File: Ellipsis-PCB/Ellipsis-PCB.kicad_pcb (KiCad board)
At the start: 2 copper layers, 114.3 x 102.4 mm, 71 parts, among them J1 Ex_Bat, J2 USB, J3 SWD, J4 Conn_02x05_Counter_Clockwise, J5 Conn_02x05_Counter_Clockwise, Q1 AO3407, Q2 AO3407, U1 E73-2G4M08S1C-52840, U2 XC6220B331MR-G, U3 MCP73831-3-OT

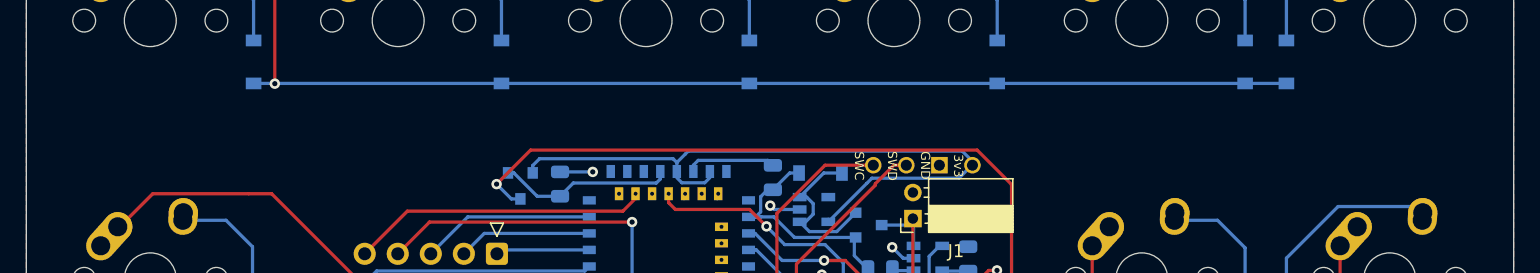
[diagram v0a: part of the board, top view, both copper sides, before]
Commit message: More things
Added mousebites and the right half
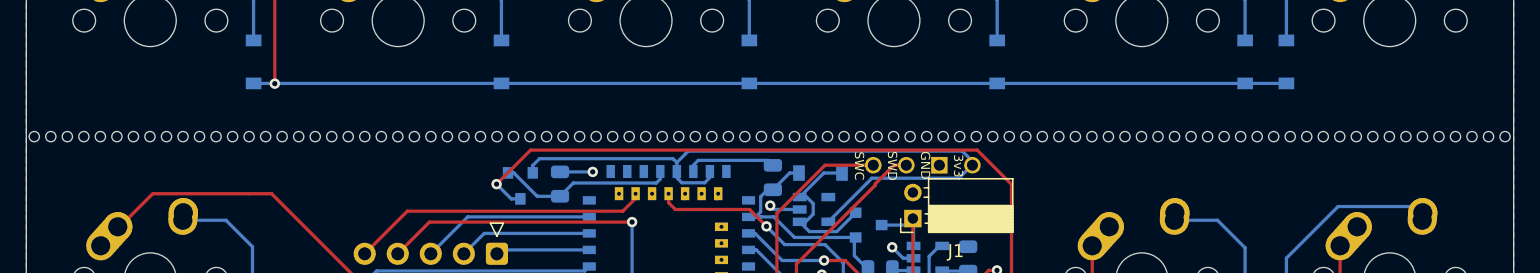
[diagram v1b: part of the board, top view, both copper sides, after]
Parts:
- added REF**: breakaway-mousebites, random-keyboard-parts:breakaway-mousebites, F.Cu at (96.0, 267.1)
- added REF**: breakaway-mousebites, random-keyboard-parts:breakaway-mousebites, F.Cu at (38.9, 267.1)
- added REF**: breakaway-mousebites, random-keyboard-parts:breakaway-mousebites, F.Cu at (51.6, 267.1)
- added REF**: breakaway-mousebites, random-keyboard-parts:breakaway-mousebites, F.Cu at (45.2, 267.1)
- added REF**: breakaway-mousebites, random-keyboard-parts:breakaway-mousebites, F.Cu at (19.8, 267.1)
- added REF**: breakaway-mousebites, random-keyboard-parts:breakaway-mousebites, F.Cu at (32.5, 267.1)
- added REF**: breakaway-mousebites, random-keyboard-parts:breakaway-mousebites, F.Cu at (26.2, 267.1)
- added REF**: breakaway-mousebites, random-keyboard-parts:breakaway-mousebites, F.Cu at (0.77, 267.1)
- added REF**: breakaway-mousebites, random-keyboard-parts:breakaway-mousebites, F.Cu at (13.5, 267.1)
- added REF**: breakaway-mousebites, random-keyboard-parts:breakaway-mousebites, F.Cu at (7.12, 267.1)
- added REF**: breakaway-mousebites, random-keyboard-parts:breakaway-mousebites, F.Cu at (108.7, 267.1)
- added REF**: breakaway-mousebites, random-keyboard-parts:breakaway-mousebites, F.Cu at (102.4, 267.1)
- added REF**: breakaway-mousebites, random-keyboard-parts:breakaway-mousebites, F.Cu at (77.0, 267.1)
- added REF**: breakaway-mousebites, random-keyboard-parts:breakaway-mousebites, F.Cu at (89.7, 267.1)
- added REF**: breakaway-mousebites, random-keyboard-parts:breakaway-mousebites, F.Cu at (83.3, 267.1)
- added REF**: breakaway-mousebites, random-keyboard-parts:breakaway-mousebites, F.Cu at (57.9, 267.1)
- added REF**: breakaway-mousebites, random-keyboard-parts:breakaway-mousebites, F.Cu at (70.6, 267.1)
- added REF**: breakaway-mousebites, random-keyboard-parts:breakaway-mousebites, F.Cu at (64.3, 267.1)
